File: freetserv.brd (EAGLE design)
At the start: 91.4 x 82.5 mm, 72 parts, among them IC2 SN75240PW, Q1 12MHz, Q2 6MHz, U1 MCP16311-E/MS

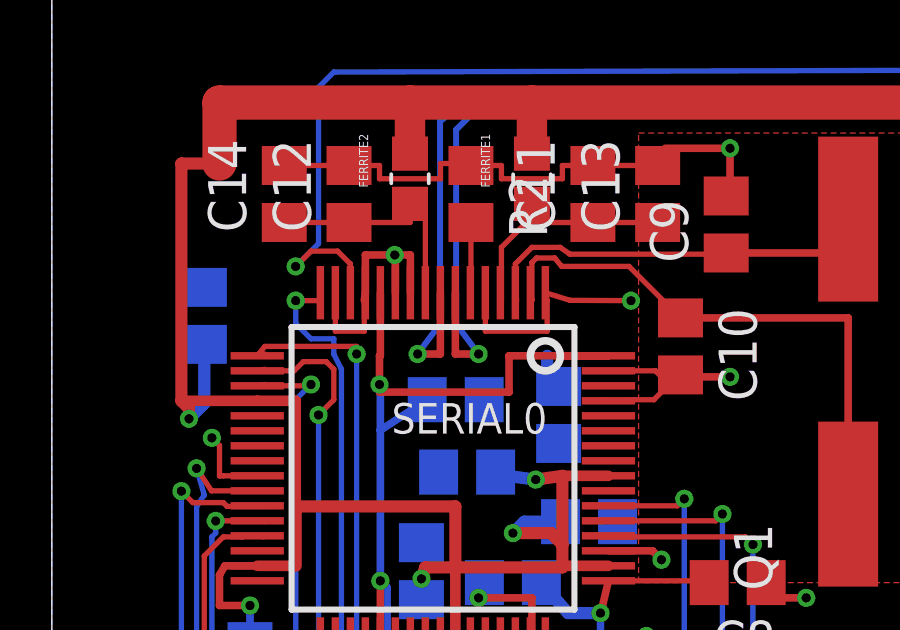
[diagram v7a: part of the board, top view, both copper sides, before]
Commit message: fix remaining airwires
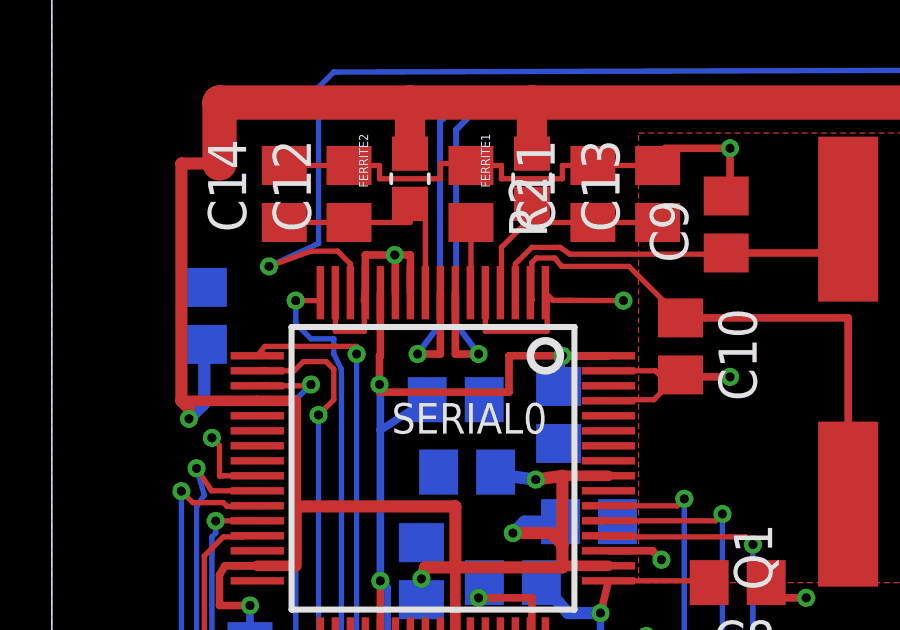
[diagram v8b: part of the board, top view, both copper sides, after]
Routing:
- net N$43: track 91.3 -> 92.8 mm
- net +1V8: track 44.2 -> 44.5 mm, vias 3 -> 4
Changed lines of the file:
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@@
 <wire x1="16.51" y1="59.182" x2="16.51" y2="60.21" width="0.1778" layer="1"/>
 <wire x1="16.51" y1="60.21" x2="16.45" y2="60.464" width="0.1778" layer="1"/>
-<via x="19.304" y="60.198" extent="1-16" drill="0.3048"/>
-<wire x1="19.304" y1="60.198" x2="17.272" y2="60.21" width="0.1778" layer="1"/>
-<wire x1="17.272" y1="60.21" x2="16.45" y2="60.464" width="0.1778" layer="1"/>
+<via x="19.05" y="60.198" extent="1-16" drill="0.3048"/>
+<wire x1="19.05" y1="60.198" x2="17.272" y2="60.21" width="0.1778" layer="1"/>
 <via x="22.606" y="57.658" extent="1-16" drill="0.3048"/>
 <wire x1="22.606" y1="57.658" x2="20.955" y2="57.658" width="0.254" layer="1"/>
@@
 <wire x1="18.554" y1="57.86" x2="20.118" y2="57.86" width="0.1778" layer="1"/>
 <wire x1="20.118" y1="57.86" x2="20.574" y2="57.404" width="0.1778" layer="1"/>
-<wire x1="11.95" y1="60.464" x2="14.45" y2="60.464" width="0" layer="19" extent="1-1"/>
+<wire x1="17.272" y1="60.21" x2="16.704" y2="60.21" width="0.1778" layer="1"/>
+<wire x1="16.704" y1="60.21" x2="16.45" y2="60.464" width="0.1778" layer="1"/>
 </signal>
 <signal name="USB0_DM_P">
@@
 <wire x1="18.288" y1="49.784" x2="18.3" y2="49.796" width="0.254" layer="1"/>
 <wire x1="18.3" y1="49.796" x2="18.554" y2="50.86" width="0.254" layer="1"/>
-<wire x1="18.554" y1="58.36" x2="15.24" y2="58.36" width="0.254" layer="1"/>
+<wire x1="18.554" y1="58.36" x2="17.018" y2="58.36" width="0.254" layer="1"/>
+<wire x1="17.018" y1="58.36" x2="15.24" y2="58.36" width="0.254" layer="1"/>
 <wire x1="15.24" y1="58.36" x2="15.24" y2="57.15" width="0.254" layer="1"/>
 <wire x1="15.24" y1="57.15" x2="10.922" y2="57.15" width="0.254" layer="1"/>
@@
 <contactref element="C39" pad="1"/>
 <wire x1="16.891" y1="57.338" x2="16.51" y2="57.592" width="0.4064" layer="16"/>
-<wire x1="16.51" y1="57.592" x2="16.51" y2="58.36" width="0.4064" layer="16"/>
 <wire x1="16.317" y1="50.8" x2="17.206" y2="49.784" width="0.4064" layer="16"/>
 <wire x1="17.206" y1="49.784" x2="18.288" y2="49.784" width="0.4064" layer="16"/>
 <wire x1="12.512" y1="56.896" x2="10.95" y2="55.88" width="0.254" layer="16"/>
-<wire x1="17.018" y1="58.36" x2="16.51" y2="58.36" width="0" layer="19" extent="1-16"/>
+<via x="17.018" y="58.36" extent="1-16" drill="0.3048"/>
+<wire x1="17.018" y1="58.36" x2="17.018" y2="57.465" width="0.1778" layer="16"/>
+<wire x1="17.018" y1="57.465" x2="16.891" y2="57.338" width="0.1778" layer="16"/>
 </signal>
 <signal name="N$14">
@@
 <wire x1="49.53" y1="68.773" x2="61.788" y2="68.834" width="0.4064" layer="1"/>
 <wire x1="61.788" y1="68.834" x2="62.23" y2="69.276" width="0.4064" layer="1"/>
-<via x="8.128" y="61.341" extent="1-16" drill="0.3048"/>
-<wire x1="8.128" y1="61.341" x2="8.636" y2="61.849" width="0.1778" layer="1"/>
+<via x="7.239" y="61.341" extent="1-16" drill="0.3048"/>
+<wire x1="7.239" y1="61.341" x2="8.636" y2="61.849" width="0.1778" layer="1"/>
 <wire x1="8.636" y1="61.849" x2="9.525" y2="61.849" width="0.1778" layer="1"/>
 <wire x1="9.525" y1="61.849" x2="9.95" y2="61.424" width="0.1778" layer="1"/>
 <wire x1="9.95" y1="61.424" x2="9.95" y2="60.464" width="0.1778" layer="1"/>
-<wire x1="8.128" y1="61.341" x2="8.89" y2="62.103" width="0.1778" layer="16"/>
+<wire x1="7.239" y1="61.341" x2="8.89" y2="62.103" width="0.1778" layer="16"/>
 <wire x1="8.89" y1="62.103" x2="8.89" y2="67.31" width="0.1778" layer="16"/>
 <wire x1="8.89" y1="67.31" x2="9.398" y2="67.818" width="0.1778" layer="16"/>
